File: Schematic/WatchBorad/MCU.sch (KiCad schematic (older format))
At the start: 1 part

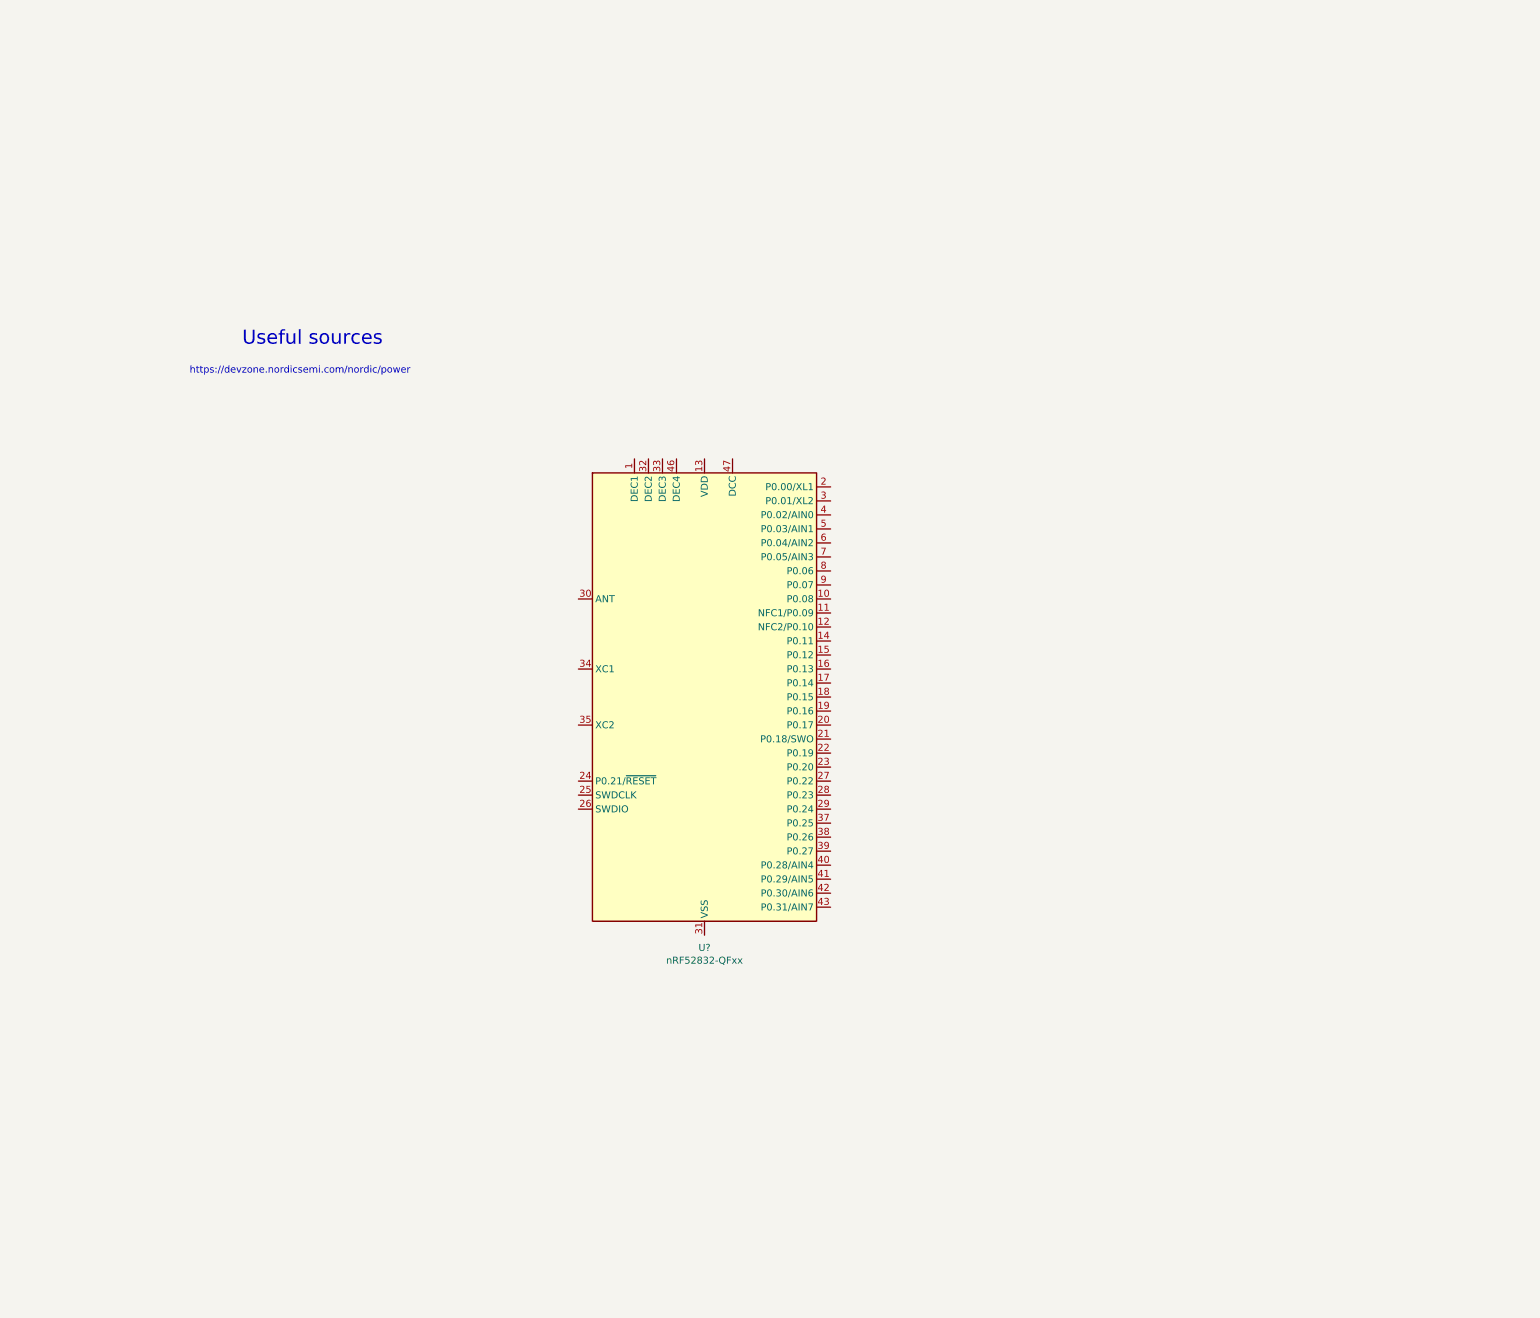
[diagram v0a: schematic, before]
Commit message: Added on/off circuit for PON and added other changes
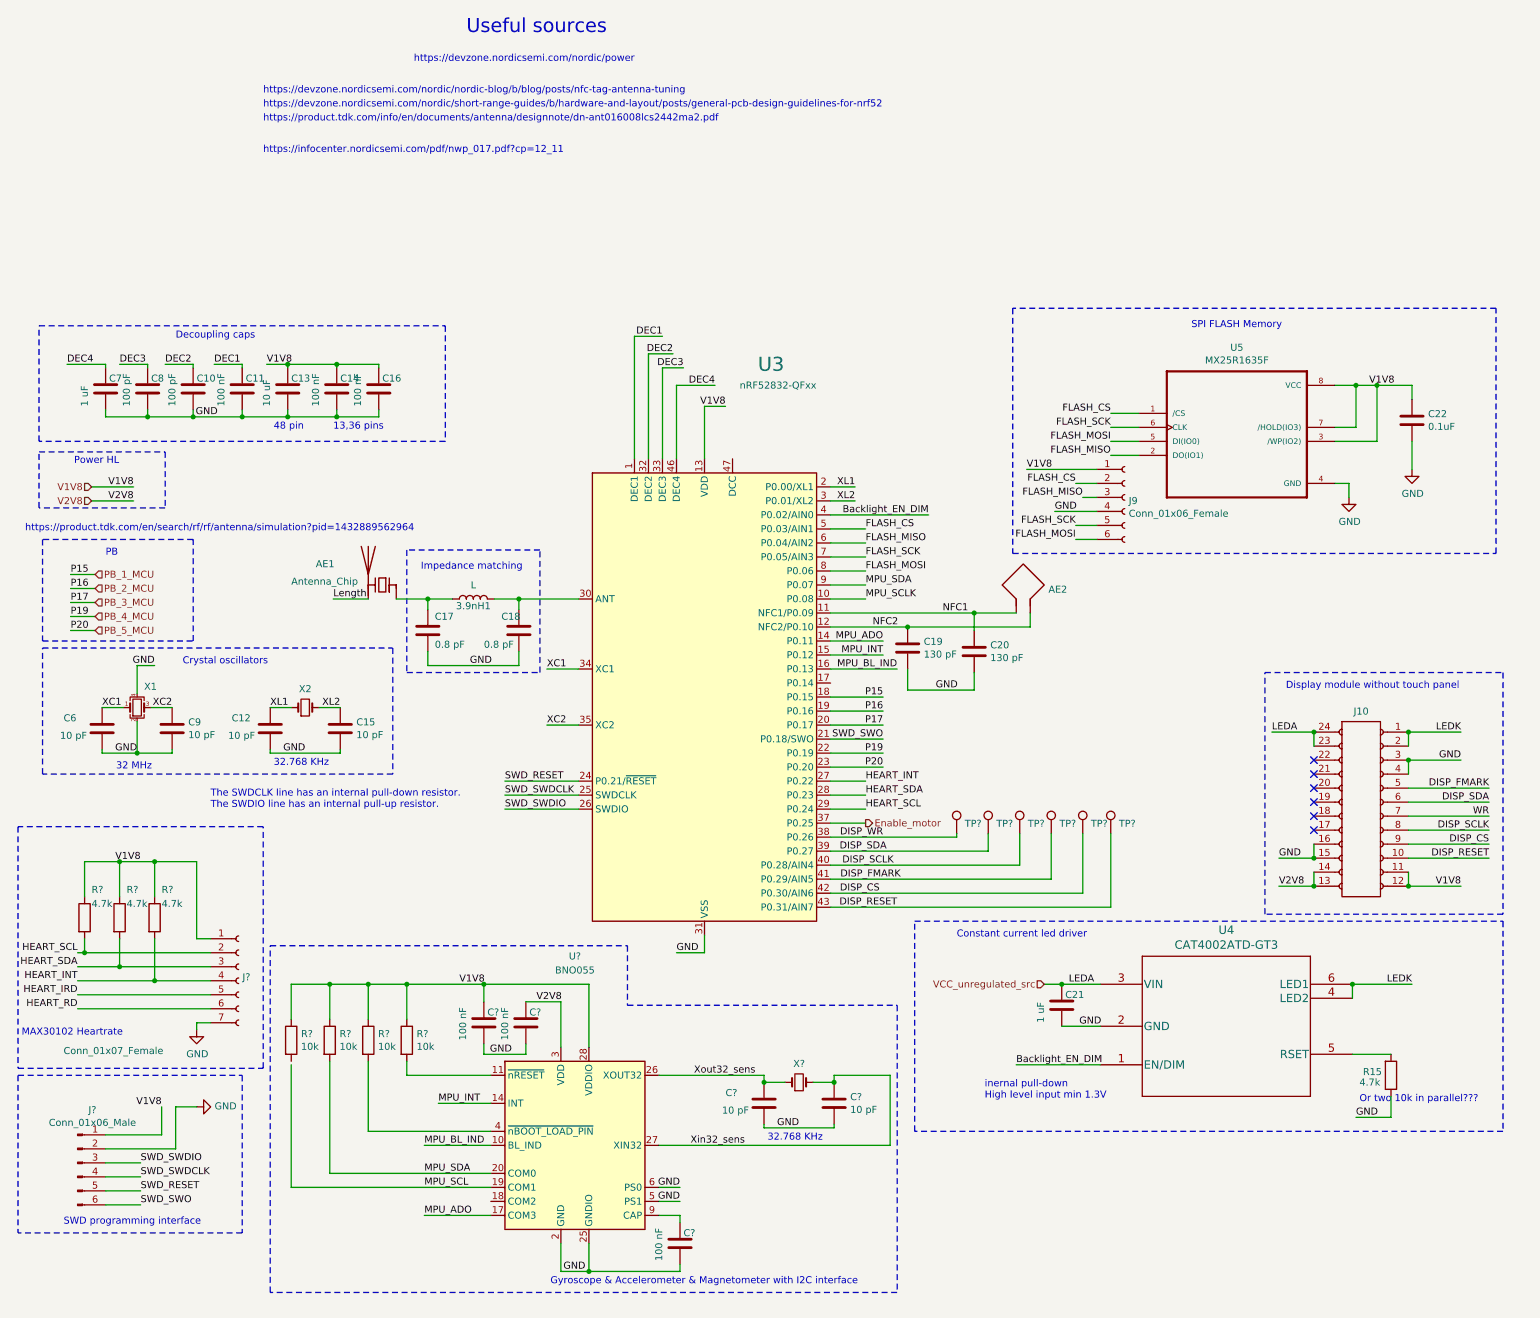
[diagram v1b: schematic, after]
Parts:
- added 3.9nH1: L, symbol Device:L
- added AE1: Antenna_Chip, symbol Device:Antenna_Chip
- added AE2: Antenna_Loop, symbol Device:Antenna_Loop
- added C10, C8: 100 pF, Capacitors_SMD:C_0603_HandSoldering, symbol Device:C
- added C11, C14, C16, C? (x3): 100 nF, Capacitors_SMD:C_0603_HandSoldering, symbol Device:C
- added C12, C15, C6, C9, C? (x2): 10 pF, symbol Device:C
- added C13: 10 uF, Capacitors_SMD:C_0603_HandSoldering, symbol Device:C
- added C17, C18: 0.8 pF, symbol Device:C
- added C19, C20: 130 pF, symbol Device:C
- added C21, C7: 1 uF, Capacitors_SMD:C_0603_HandSoldering, symbol Device:C
- added C22: 0.1uF, Capacitors_SMD:C_0603_HandSoldering, symbol Device:C
- added J10: DF37NC-24DS-0.4V(51)_Female, symbol Hirose_connectors:DF37NC-24DS-0.4V(51)_Female
- added J9: Conn_01x06_Female, Connector_PinSocket_2.54mm:PinSocket_1x06_P2.54mm_Vertical, symbol Connector:Conn_01x06_Female
- added J?: Conn_01x07_Female, Connector_PinSocket_2.54mm:PinSocket_1x07_P2.54mm_Vertical, symbol Connector:Conn_01x07_Female
- added J?: Conn_01x06_Male, Connector_PinHeader_2.54mm:PinHeader_1x06_P2.54mm_Vertical, symbol Connector:Conn_01x06_Male
- added R15: 4.7k, Resistors_SMD:R_0603_HandSoldering, symbol Device:R
- added R? (x3): 4.7k, Resistor_SMD:R_0805_2012Metric, symbol Device:R
- added R? (x4): 10k, Resistors_SMD:R_0603_HandSoldering, symbol Device:R
- added TP? (x6): TestPoint, testpoints:testpoint, symbol Connector:TestPoint
- added U4: CAT4002ATD-GT3, TSOT23-6, symbol LocalLedDrivers:CAT4002ATD-GT3
- added U5: MX25R1635F, symbol W25Q16BVSSIG:MX25R1635F
- added U?: BNO055, Package_LGA:LGA-28_5.2x3.8mm_P0.5mm, symbol Sensor_Motion:BNO055
- added X1: Crystal_GND24_Small, Crystals:Crystal_SMD_2016-4pin_2.0x1.6mm, symbol Device:Crystal_GND24_Small
- added X2, X?: Crystal_Small, Crystals:Crystal_SMD_2012-2pin_2.0x1.2mm, symbol Device:Crystal_Small
- gave numbers to parts that had none: 1
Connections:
- net DEC1: now reaches U3.1 (DEC1)
- net DEC1: now also C11.1
- net MPU_SCLK: now reaches U3.10 (P0.08)
- net NFC1: now reaches U3.11 (NFC1/P0.09)
- net NFC1: now also AE2.1, C20.1
- net NFC2: now reaches U3.12 (NFC2/P0.10)
- net NFC2: now also AE2.2, C19.1
- net V1V8: now reaches U3.13 (VDD), U3.36 (VDD), U3.48 (VDD)
- net V1V8: now also C13.1, C14.1, C16.1, C22.1, C?.1, J10.11 (Pin_11), J10.12 (Pin_12), J9.1 (Pin_1), J?.1 (Pin_1), J?.1 (Pin_1), R?.1, R?.1, R?.1, R?.1, R?.1, R?.1, R?.1, U5.3 (/WP(IO2)), U5.7 (/HOLD(IO3)), U5.8 (VCC), U?.28 (VDDIO)
- net MPU_ADO: now reaches U3.14 (P0.11)
- net MPU_ADO: now also U?.17 (COM3)
- net MPU_INT: now reaches U3.15 (P0.12)
- net MPU_INT: now also U?.14 (INT)
- net MPU_BL_IND: now reaches U3.16 (P0.13)
- net MPU_BL_IND: now also U?.10 (BL_IND)
- net PB_1_MCU: now reaches U3.18 (P0.15)
- net PB_2_MCU: now reaches U3.19 (P0.16)
- net XL1: now reaches U3.2 (P0.00/XL1)
- net XL1: now also C12.1, X2.1
- net PB_3_MCU: now reaches U3.20 (P0.17)
- net SWD_SWO: now reaches U3.21 (P0.18/SWO)
- net SWD_SWO: now also J?.6 (Pin_6)
- net PB_4_MCU: now reaches U3.22 (P0.19)
- net PB_5_MCU: now reaches U3.23 (P0.20)
- net SWD_RESET: now reaches U3.24 (P0.21/~RESET)
- net SWD_RESET: now also J?.5 (Pin_5)
- net SWD_SWDCLK: now reaches U3.25 (SWDCLK)
- net SWD_SWDCLK: now also J?.4 (Pin_4)
- net SWD_SWDIO: now reaches U3.26 (SWDIO)
- net SWD_SWDIO: now also J?.3 (Pin_3)
- net HEART_INT: now reaches U3.27 (P0.22)
- net HEART_INT: now also J?.4 (Pin_4), R?.2
- net HEART_SDA: now reaches U3.28 (P0.23)
- net HEART_SDA: now also J?.3 (Pin_3), R?.2
- net HEART_SCL: now reaches U3.29 (P0.24)
- net HEART_SCL: now also J?.2 (Pin_2), R?.2
- net XL2: now reaches U3.3 (P0.01/XL2)
- net XL2: now also C15.1, X2.2
- net at U3.30 (ANT): now also 3.9nH1.2, C18.1
- net GND: now reaches U3.31 (VSS), U3.45 (VSS), U3.49 (VSS)
- net GND: now also C10.2, C11.2, C12.2, C13.2, C14.2, C15.2, C16.2, C17.2, C18.2, C19.2, C20.2, C21.2, C22.2, C6.2, C7.2, C8.2, C9.2, C?.2, C?.2, C?.2, C?.2, C?.2, J10.15 (Pin_15), J10.16 (Pin_16), J10.3 (Pin_3), J10.4 (Pin_4), J9.4 (Pin_4), J?.2 (Pin_2), J?.7 (Pin_7), R15.1, U4.2 (GND), U5.4 (GND), U?.15 (GNDIO), U?.16 (GNDIO), U?.2 (GND), U?.25 (GNDIO), U?.5 (PS1), U?.6 (PS0), X1.2, X1.4
- net DEC2: now reaches U3.32 (DEC2)
- net DEC2: now also C10.1
- net DEC3: now reaches U3.33 (DEC3)
- net DEC3: now also C8.1
- net XC1: now reaches U3.34 (XC1)
- net XC1: now also C6.1, X1.1
- net XC2: now reaches U3.35 (XC2)
- net XC2: now also C9.1, X1.3
- net Enable_motor: now reaches U3.37 (P0.25)
- net DISP_WR: now reaches U3.38 (P0.26)
- net DISP_WR: now also TP?.1
- net DISP_SDA: now reaches U3.39 (P0.27)
- net DISP_SDA: now also J10.6 (Pin_6), TP?.1
- net Backlight_EN_DIM: now reaches U3.4 (P0.02/AIN0)
- net Backlight_EN_DIM: now also U4.1 (EN/DIM)
- net DISP_SCLK: now reaches U3.40 (P0.28/AIN4)
- net DISP_SCLK: now also J10.8 (Pin_8), TP?.1
- net DISP_FMARK: now reaches U3.41 (P0.29/AIN5)
- net DISP_FMARK: now also J10.5 (Pin_5), TP?.1
- net DISP_CS: now reaches U3.42 (P0.30/AIN6)
- net DISP_CS: now also J10.9 (Pin_9), TP?.1
- net DISP_RESET: now reaches U3.43 (P0.31/AIN7)
- net DISP_RESET: now also J10.10 (Pin_10), TP?.1
- net DEC4: now reaches U3.46 (DEC4)
- net DEC4: now also C7.1
- net FLASH_CS: now reaches U3.5 (P0.03/AIN1)
- net FLASH_CS: now also J9.2 (Pin_2), U5.1 (/CS)
- net FLASH_MISO: now reaches U3.6 (P0.04/AIN2)
- net FLASH_MISO: now also J9.3 (Pin_3), U5.2 (DO(IO1))
- net FLASH_SCK: now reaches U3.7 (P0.05/AIN3)
- net FLASH_SCK: now also J9.5 (Pin_5), U5.6 (CLK)
- net FLASH_MOSI: now reaches U3.8 (P0.06)
- net FLASH_MOSI: now also J9.6 (Pin_6), U5.5 (DI(IO0))
- net MPU_SDA: now reaches U3.9 (P0.07)
- net MPU_SDA: now also R?.2, U?.20 (COM0)
- new net: 3.9nH1.1, AE1.1 (FEED), C17.1
- new net: R15.2, U4.5 (RSET)
- new net: R?.2, U?.11 (~nRESET)
- new net: R?.2, U?.4 (~nBOOT_LOAD_PIN)
- new net: C?.1, U?.9 (CAP)
- new net HEART_IRD: J?.5 (Pin_5)
- new net HEART_RD: J?.6 (Pin_6)
- new net LEDK: J10.1 (Pin_1), J10.2 (Pin_2), U4.4 (LED2), U4.6 (LED1)
- new net Length: AE1.2 (PCB_Trace)
- new net MPU_SCL: U?.19 (COM1)
- new net V2V8: C?.1, J10.13 (Pin_13), J10.14 (Pin_14), U?.3 (VDD)
- new net VCC_unregulated_src: C21.1, J10.23 (Pin_23), J10.24 (Pin_24), U4.3 (VIN)
- new net WR: J10.7 (Pin_7)
- new net Xin32_sens: C?.1, U?.27 (XIN32), X?.2
- new net Xout32_sens: C?.1, U?.26 (XOUT32), X?.1
- no-connect marks 0 -> 6
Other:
- note added: "13,36 pins\n"
- note added: "32 MHz"
- note added: "32.768 KHz\n"
- note added: "48 pin\n"
- note added: "Constant current led driver\n"
- note added: "Crystal oscillators"
- note added: "Decoupling caps\n"
- note added: "Display module without touch panel\n"
- note added: "Gyroscope & Accelerometer & Magnetometer with I2C interface"
- note added: "Impedance matching"
- note added: "MAX30102 Heartrate"
- note added: "Or two 10k in parallel???\n"
- note added: "PB\n"
- note added: "Power HL\n\n"
- note added: "SPI FLASH Memory\n"
- note added: "SWD programming interface"
- note added: "The SWDCLK line has an internal pull-down resistor.\nThe SWDIO line has an internal pull-up resistor.\n"
- note added: "https://devzone.nordicsemi.com/nordic/nordic-blog/b/blog/posts/nfc-tag-antenna-tuning"
- note added: "https://devzone.nordicsemi.com/nordic/short-range-guides/b/hardware-and-layout/posts/general-pcb-design-guidelines-for-nrf52"
- note added: "https://infocenter.nordicsemi.com/pdf/nwp_017.pdf?cp=12_11"
- note added: "https://product.tdk.com/en/search/rf/rf/antenna/simulation?pid=1432889562964"
- note added: "https://product.tdk.com/info/en/documents/antenna/designnote/dn-ant016008lcs2442ma2.pdf"
- note added: "inernal pull-down\nHigh level input min 1.3V"

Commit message: Display is replaced, now it has single power supply. One PSU is removed. Circuit PB is modified.
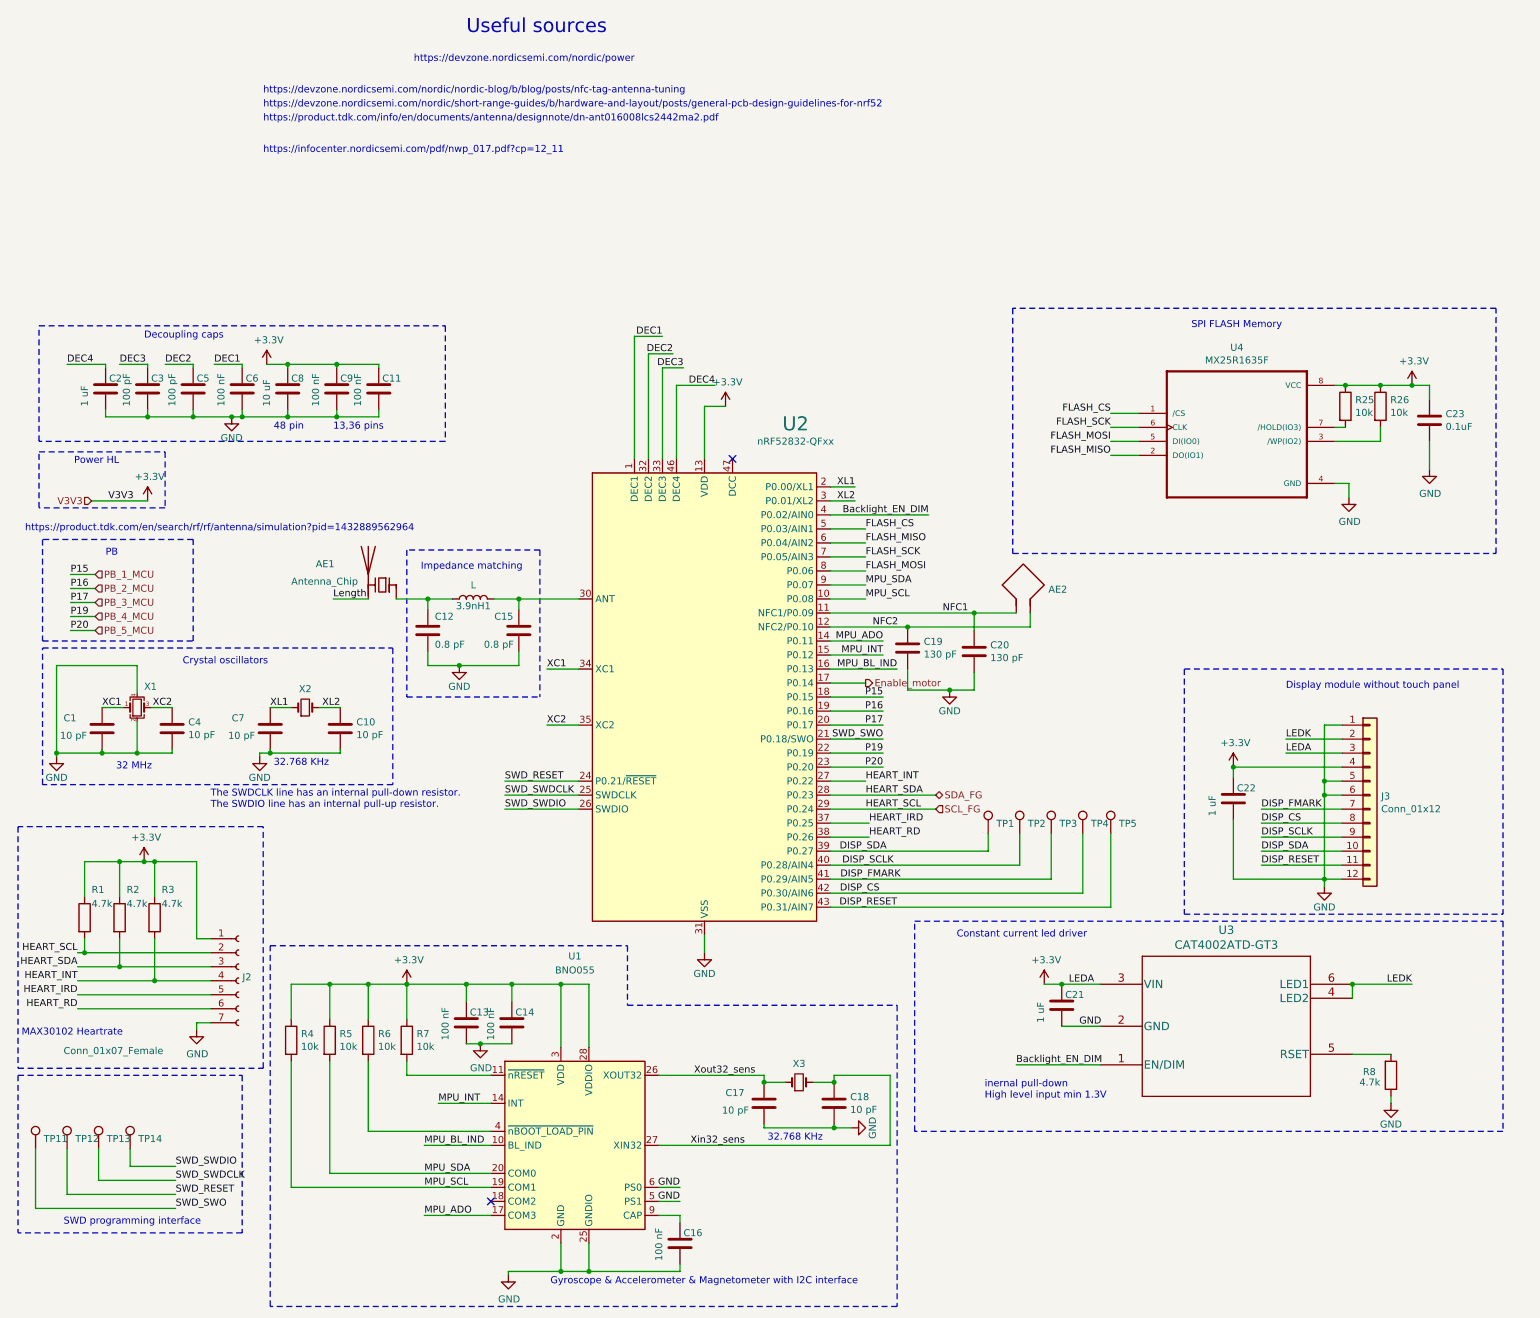
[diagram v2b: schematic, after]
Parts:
- removed J10: DF37NC-24DS-0.4V(51)_Female, symbol Hirose_connectors:DF37NC-24DS-0.4V(51)_Female
- removed J9: Conn_01x06_Female, Connector_PinSocket_2.54mm:PinSocket_1x06_P2.54mm_Vertical, symbol Connector:Conn_01x06_Female
- removed J?: Conn_01x06_Male, Connector_PinHeader_2.54mm:PinHeader_1x06_P2.54mm_Vertical, symbol Connector:Conn_01x06_Male
- removed TP?: TestPoint, testpoints:testpoint, symbol Connector:TestPoint
- added C22: 1 uF, Capacitors_SMD:C_0603_HandSoldering, symbol Device:C
- added J3: Conn_01x12, symbol Connector_Generic:Conn_01x12
- added R25, R26: 10k, Resistors_SMD:R_0603_HandSoldering, symbol Device:R
- added TP11, TP12, TP13, TP14: TestPoint, Measurement_Points:Measurement_Point_Round-SMD-Pad_Small, symbol Connector:TestPoint
- 3.9nH1, AE1, C19, C20: footprint (none) -> Capacitors_SMD:C_0603_HandSoldering
- C1: renamed from C6; footprint (none) -> Capacitors_SMD:C_0603_HandSoldering
- C10: renamed from C15; footprint (none) -> Capacitors_SMD:C_0603_HandSoldering
- C12: renamed from C17; footprint (none) -> Capacitors_SMD:C_0603_HandSoldering
- C15: renamed from C18; footprint (none) -> Capacitors_SMD:C_0603_HandSoldering
- C17, C18: renamed from C?; footprint (none) -> Capacitors_SMD:C_0603_HandSoldering
- C4: renamed from C9; footprint (none) -> Capacitors_SMD:C_0603_HandSoldering
- C7: renamed from C12; footprint (none) -> Capacitors_SMD:C_0603_HandSoldering
- R1, R2, R3: renamed from R?; footprint Resistor_SMD:R_0805_2012Metric -> Resistors_SMD:R_0603_HandSoldering
- TP1, TP2, TP3, TP4, TP5: renamed from TP?; footprint testpoints:testpoint -> Measurement_Points:Measurement_Point_Round-SMD-Pad_Small
- U1: renamed from U?; footprint Package_LGA:LGA-28_5.2x3.8mm_P0.5mm -> Housings_LGA:LGA-28_5.2x3.8mm_Pitch0.5mm
- U2: renamed from U3; footprint Package_DFN_QFN:QFN-48-1EP_6x6mm_P0.4mm_EP4.6x4.6mm -> Housings_DFN_QFN:QFN-48-1EP_6x6mm_Pitch0.4mm
- U3: renamed from U4; footprint TSOT23-6 -> TO_SOT_Packages_SMD:SOT-23-6_Handsoldering
- U4: renamed from U5; footprint (none) -> SMD_Packages:SOIC-8-N
- gave numbers to parts that had none: 9
- renumbered C16 to C11, C7 to C2, C22 to C23, C8 to C3, C10 to C5, C11 to C6, C13 to C8, C14 to C9, R15 to R8
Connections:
- net DISP_WR is gone; now on net HEART_RD: U2.38 (P0.26)
- net MPU_SCLK is gone; now on net MPU_SCL: U2.10 (P0.08)
- net V2V8 is gone; now on net +3V3: C14.1, U1.3 (VDD)
- net VCC_unregulated_src is gone; now on net +3V3: C21.1, U3.3 (VIN)
- net DISP_CS: now also J3.8 (Pin_8)
- net DISP_FMARK: now also J3.7 (Pin_7)
- net DISP_RESET: now also J3.11 (Pin_11)
- net DISP_SCLK: now also J3.9 (Pin_9)
- net DISP_SDA: now also J3.10 (Pin_10)
- net Enable_motor: now also U2.17 (P0.14); no longer U2.37 (P0.25)
- net GND: now also C22.2, J3.1 (Pin_1), J3.12 (Pin_12), J3.5 (Pin_5), J3.6 (Pin_6)
- net HEART_IRD: now also U2.37 (P0.25)
- net LEDK: now also J3.2 (Pin_2)
- net MPU_SCL: now also R4.2
- net SWD_RESET: now also TP12.1
- net SWD_SWDCLK: now also TP13.1
- net SWD_SWDIO: now also TP14.1
- net SWD_SWO: now also TP11.1
- net HEART_SCL renamed SCL_FG
- net HEART_SDA renamed SDA_FG
- net V1V8 renamed +3V3
- net +3V3: now also C22.1, J3.3 (Pin_3), J3.4 (Pin_4), R25.1, R26.1; no longer U4.3 (/WP(IO2)), U4.7 (/HOLD(IO3))
- new net: R26.2, U4.3 (/WP(IO2))
- new net: R25.2, U4.7 (/HOLD(IO3))
- no-connect marks 6 -> 2
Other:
- note removed: "Or two 10k in parallel???\n"
- moved on the sheet: C13, C14, C23
